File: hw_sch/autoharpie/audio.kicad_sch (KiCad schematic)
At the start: 2 parts, among them J10 AudioJack3, U18 SGTL5000XNLA3R2

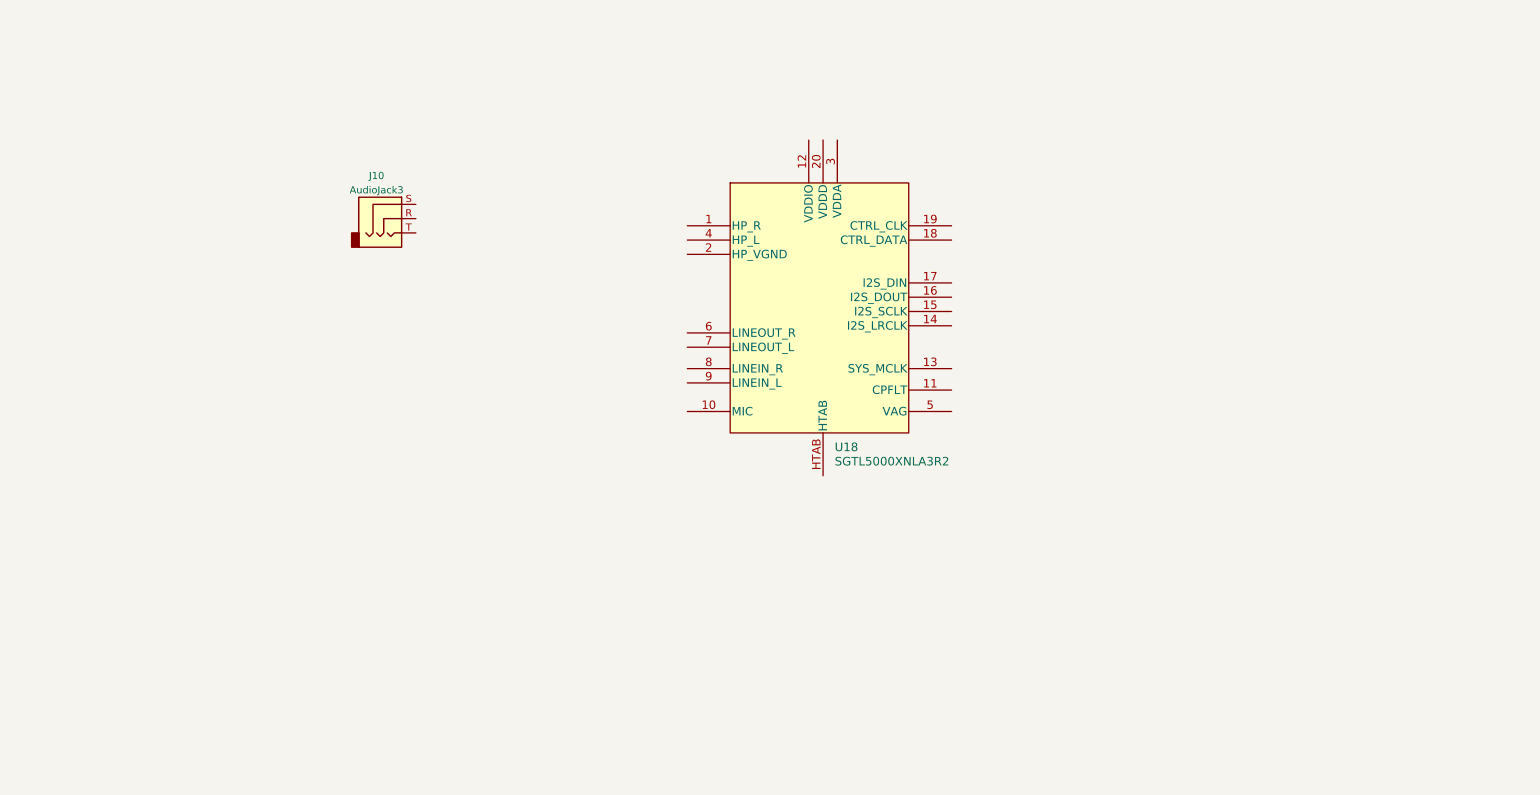
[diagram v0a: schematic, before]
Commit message: DAC wiring, add heirch pins
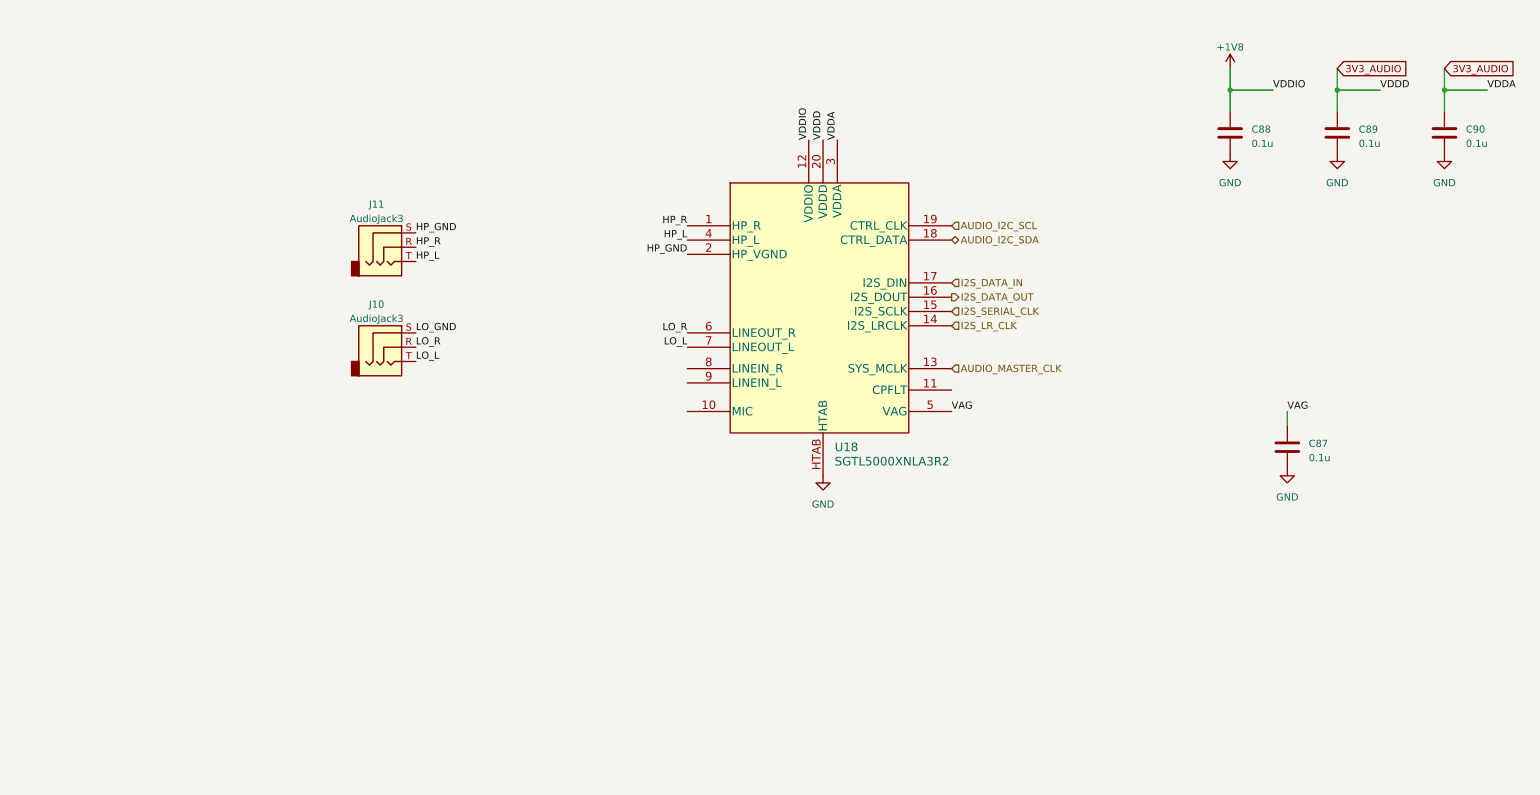
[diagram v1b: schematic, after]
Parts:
- added C87, C88, C89, C90: 0.1u, symbol Device:C
- added J11: AudioJack3, Connector_Audio:Jack_3.5mm_CUI_SJ-3524-SMT_Horizontal, symbol Connector_Audio:AudioJack3
- J10: footprint Connector_Audio:Jack_3.5mm_CUI_SJ-3524-SMT_Horizontal -> (none)
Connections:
- net HP_R: now reaches U18.1 (HP_R)
- net HP_R: now also J11.R
- net +1V8: now reaches U18.12 (VDDIO)
- net +1V8: now also C88.1
- net AUDIO_MASTER_CLK: now reaches U18.13 (SYS_MCLK)
- net I2S_LR_CLK: now reaches U18.14 (I2S_LRCLK)
- net I2S_SERIAL_CLK: now reaches U18.15 (I2S_SCLK)
- net I2S_DATA_OUT: now reaches U18.16 (I2S_DOUT)
- net I2S_DATA_IN: now reaches U18.17 (I2S_DIN)
- net AUDIO_I2C_SDA: now reaches U18.18 (CTRL_DATA)
- net AUDIO_I2C_SCL: now reaches U18.19 (CTRL_CLK)
- net HP_GND: now reaches U18.2 (HP_VGND)
- net HP_GND: now also J11.S
- net 3V3_AUDIO: now reaches U18.20 (VDDD)
- net 3V3_AUDIO: now also U18.3 (VDDA), C89.1, C90.1
- net HP_L: now reaches U18.4 (HP_L)
- net HP_L: now also J11.T
- net VAG: now reaches U18.5 (VAG)
- net VAG: now also C87.1
- net LO_R: now reaches U18.6 (LINEOUT_R)
- net LO_R: now also J10.R
- net LO_L: now reaches U18.7 (LINEOUT_L)
- net LO_L: now also J10.T
- net GND: now reaches U18.HTAB
- net GND: now also C87.2, C88.2, C89.2, C90.2
- net LO_GND: now reaches J10.S

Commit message: keypad
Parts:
- removed J10: AudioJack3, symbol Connector_Audio:AudioJack3
- removed J11: AudioJack3, Connector_Audio:Jack_3.5mm_CUI_SJ-3524-SMT_Horizontal, symbol Connector_Audio:AudioJack3
- added J10: Conn_01x02_Pin, Connector_PinSocket_2.54mm:PinSocket_1x02_P2.54mm_Vertical, symbol Connector:Conn_01x02_Pin
- added J11, J9: AudioJack3_SwitchTR, Connector_Audio:Jack_3.5mm_CUI_SJ1-3535NG_Horizontal_CircularHoles, symbol Connector_Audio:AudioJack3_SwitchTR
- added R36, R37: 1k, Resistor_THT:R_Axial_DIN0204_L3.6mm_D1.6mm_P7.62mm_Horizontal, symbol Device:R
- C76: renamed from C88; footprint (none) -> Capacitor_SMD:C_0402_1005Metric
- C77: renamed from C89; footprint (none) -> Capacitor_SMD:C_0402_1005Metric
- C78: renamed from C90; footprint (none) -> Capacitor_SMD:C_0402_1005Metric
- C79: renamed from C87; footprint (none) -> Capacitor_SMD:C_0402_1005Metric
- U7: renamed from U18; footprint QFN20_FRE -> footprints2:SGTL5000XNLA3R2
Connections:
- net HP_GND: now also J10.2 (Pin_2), J9.S
- net HP_L: now also J9.T
- net HP_R: now also J9.R
- net LO_GND: now also J11.S
- net LO_L: now also J11.T
- net LO_R: now also J11.R
- new net: J10.1 (Pin_1), R36.1
- new net: J9.RN, J9.TN, R36.2, R37.1, R37.2
- no-connect marks 0 -> 6

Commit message: rev 0.1 pcb
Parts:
- removed J10: Conn_01x02_Pin, Connector_PinSocket_2.54mm:PinSocket_1x02_P2.54mm_Vertical, symbol Connector:Conn_01x02_Pin
- added C52, C53: 220u, Capacitor_THT:C_Disc_D7.0mm_W2.5mm_P5.00mm, symbol Device:C
- added C54, C55: 1u, Capacitor_THT:C_Disc_D7.0mm_W2.5mm_P5.00mm, symbol Device:C
- added J7: Conn_01x02_Pin, Connector_JST:JST_PH_S2B-PH-K_1x02_P2.00mm_Horizontal, symbol Connector:Conn_01x02_Pin
- renumbered C76 to C49, C77 to C50, C78 to C51, C79 to C56, J9 to J6, J11 to J8, R36 to R13, R37 to R14
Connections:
- net LO_GND is gone; now on net GND: J8.S
- net HP_GND: now also J7.1 (Pin_1)
- net HP_L: now also C53.2; no longer J6.T
- net HP_R: now also C52.2; no longer J6.R
- net LO_L: now also C55.2; no longer J8.T
- net LO_R: now also C54.2; no longer J8.R
- net at R13.1: now also J7.2 (Pin_2)
- net at J6.TN, R13.2, R14.1: no longer J6.RN, R14.2
- net 3V3_AUDIO renamed +3V3
- new net: C52.1, J6.R
- new net: C54.1, J8.R
- new net: C55.1, J8.T
- new net: C53.1, J6.T
- new net: J6.RN, R14.2

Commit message: ic fix atept
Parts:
- removed C52, C53: 220u, Capacitor_THT:C_Disc_D7.0mm_W2.5mm_P5.00mm, symbol Device:C
- renumbered C49 to C38, C50 to C39, C51 to C40, C54 to C41, C55 to C42, C56 to C43, R13 to R15, R14 to R16, U7 to U8
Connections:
- net HP_L: now also J6.T
- net HP_R: now also J6.R
- net I2S_DATA_OUT: no longer names the net of U8.16 (I2S_DOUT)
- no-connect marks 6 -> 7

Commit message: new icc
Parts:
- removed J8: AudioJack3_SwitchTR, Connector_Audio:Jack_3.5mm_CUI_SJ1-3535NG_Horizontal_CircularHoles, symbol Connector_Audio:AudioJack3_SwitchTR
- removed U8: SGTL5000XNLA3R2, footprints2:SGTL5000XNLA3R2, symbol 2023-03-10_05-17-13:SGTL5000XNLA3R2
- added C43: 220u, Capacitor_SMD:C_0805_2012Metric, symbol Device:C
- added C44, C45, C48, C49: 1u, Capacitor_SMD:C_0603_1608Metric, symbol Device:C
- added C47: 2.2u, Capacitor_SMD:C_0805_2012Metric, symbol Device:C
- added U8: MAX9867ETJ+T, max:QFN50P500X500X80-33N, symbol MAX9867ETJ+T:MAX9867ETJ+T
- C38, C39, C40: value 0.1u -> 1u; footprint Capacitor_SMD:C_0402_1005Metric -> Capacitor_SMD:C_0603_1608Metric
- C41: footprint Capacitor_THT:C_Disc_D7.0mm_W2.5mm_P5.00mm -> Capacitor_SMD:C_0603_1608Metric
- C42: value 1u -> 220u; footprint Capacitor_THT:C_Disc_D7.0mm_W2.5mm_P5.00mm -> Capacitor_SMD:C_0805_2012Metric
- C46: renamed from C43; value 0.1u -> 1u; footprint Capacitor_SMD:C_0402_1005Metric -> Capacitor_SMD:C_0603_1608Metric
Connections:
- net HP_R is gone; now on an unnamed net: J6.R
- net +1V8: now also C39.1, C40.1, U8.23 (PVDD), U8.32 (DVDD), U8.5 (AVDD)
- net +3V3: now also C41.1, U8.26 (DVDDIO); no longer C39.1, C40.1
- net AUDIO_I2C_SCL: now also U8.2 (SCL)
- net AUDIO_I2C_SDA: now also U8.3 (SDA)
- net AUDIO_MASTER_CLK: now also U8.31 (MCLK)
- net GND: now also C47.2, C48.2, U8.1 (DGND); no longer C38.2
- net I2S_DATA_IN: now also U8.28 (SDIN)
- net I2S_LR_CLK: now also U8.29 (LRCLK)
- net I2S_SERIAL_CLK: now also U8.30 (BCLK)
- net HP_GND: no longer names the net of J7.1 (Pin_1)
- net HP_GND: now also C49.1; no longer J6.S
- net HP_L: no longer names the net of J6.T
- net HP_L: now also C43.1
- net LO_L renamed RIGHT
- net RIGHT: now also U8.19 (ROUTP)
- net LO_R renamed AGND
- net AGND: now also C38.2, J6.S, C44.2, C45.2, C49.2, U8.18 (PGND), U8.33 (EP), U8.9 (AGND)
- net VAG renamed PREG
- net PREG: now also U8.7 (PREG)
- new net INT: U8.4 (~{IRQ})
- new net LEFT: C43.2, U8.22 (LOUTP)
- new net LOUT_AGND: C45.1, U8.21 (LOUTN)
- new net REF: C47.1, U8.6 (REF)
- new net REG: C48.1, U8.8 (REG)
- new net ROUT_AGND: C44.1, U8.20 (ROUTN)
- no-connect marks 7 -> 10
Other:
- moved on the sheet: J6, J7, R15, R16

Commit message: final final final 0.1 rev
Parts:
- added C5, C6: 1u, Capacitor_SMD:C_0603_1608Metric, symbol Device:C
- added U5: AP2112K-1.8, Package_TO_SOT_SMD:SOT-23-5, symbol Regulator_Linear:AP2112K-1.8
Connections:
- net AGND is gone; now on net GND: C38.2, C41.2, C44.2, C45.2, C49.2, J6.S, U8.18 (PGND), U8.33 (EP), U8.9 (AGND)
- net +1V8: now also C6.1, U5.5 (VOUT)
- net +3V3: now also C5.1, U5.1 (VIN), U5.3 (EN)
- net GND: now also C5.2, C6.2, U5.2 (GND)
- no-connect marks 10 -> 11

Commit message: erhtj
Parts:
- C42, C43: footprint Capacitor_SMD:C_0805_2012Metric -> Capacitor_SMD:C_1206_3216Metric
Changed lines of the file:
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@@
       (effects (font (size 1.27 1.27)))
     )
-    (property "Footprint" "Capacitor_SMD:C_0805_2012Metric" (at 81.28 61.2648 0)
+    (property "Footprint" "Capacitor_SMD:C_1206_3216Metric" (at 81.28 61.2648 0)
       (effects (font (size 1.27 1.27)) hide)
     )
@@
       (effects (font (size 1.27 1.27)))
     )
-    (property "Footprint" "Capacitor_SMD:C_0805_2012Metric" (at 81.28 72.6948 0)
-      (effects (font (size 1.27 1.27)) hide)
-    )
+    (property "Footprint" "Capacitor_SMD:C_1206_3216Metric" (at 81.28 72.6948 0)
+      (effects (font (size 1.27 1.27)) hide)
+    )
